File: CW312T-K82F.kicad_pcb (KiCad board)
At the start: 2 copper layers, 58.7 x 53.7 mm, 21 parts, among them J1 20_pin, P1 PCIEx4 EDGE CONNECTOR, U1 MK82FN256VLL15

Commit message: updated schematic and pcb - ready for review
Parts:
- moved R1 3.40 mm to (167.8, 86.7)
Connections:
- net /CW312T_Connector/nRST renamed nRST
- net /K82/JTAG_TCK renamed JTAG_TCK
- net /K82/JTAG_TDI renamed JTAG_TDI
- net /K82/JTAG_TDO renamed JTAG_TDO
- net /K82/JTAG_TMS renamed JTAG_TMS
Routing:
- net /CW312T_Connector/FILT_HP: track 35.0 -> 41.8 mm

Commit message: updated silkscreen and production files
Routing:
- net /CW312T_Connector/HDR1: track 22.1 -> 23.6 mm
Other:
- board text added: "K82F Target Board For ChipWhisperer CW312 Board"
- board text added: "RST"
- board text added: "VREF"
- board text removed: "K82F Target Board For ChipWhisperer CW312"
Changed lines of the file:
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@@
 		(tags "Surface mounted pin header SMD 2x10 1.00mm double row")
 		(property "Reference" "J1"
-			(at -2.85 -6.2 0)
+			(at -0.1 -6.25 0)
 			(layer "F.SilkS")
 			(effects
@@
 		)
 	)
+	(gr_line
+		(start 138.6 71)
+		(end 138.6 71.65)
+		(stroke
+			(width 0.15)
+			(type default)
+		)
+		(layer "B.SilkS")
+	)
+	(gr_line
+		(start 161.6 71.025)
+		(end 161.6 71.675)
+		(stroke
+			(width 0.15)
+			(type default)
+		)
+		(layer "F.SilkS")
+	)
 	(gr_text "NewAE Technology Inc. \nNAE-CW312T-K82F"
 		(at 154.8 92.25 0)
@@
 		)
 	)
-	(gr_text "K82F Target Board\nFor ChipWhisperer \nCW312"
-		(at 132.65 79.7 0)
+	(gr_text "RST"
+		(at 137.9 74.45 270)
+		(layer "B.SilkS")
+		(effects
+			(font
+				(size 1 1)
+				(thickness 0.15)
+			)
+			(justify left bottom mirror)
+		)
+	)
+	(gr_text "K82F Target Board\nFor ChipWhisperer \nCW312 Board"
+		(at 132.75 80.4 0)
 		(layer "F.SilkS")
 		(effects
@@
 		)
 	)
+	(gr_text "VREF"
+		(at 162.25 75.45 90)
+		(layer "F.SilkS")
+		(effects
+			(font
+				(size 1 1)
+				(thickness 0.15)
+			)
+			(justify left bottom)
+		)
+	)
 	(segment
 		(start 131.75 107.75)
@@
 		(start 167.024999 97.324999)
 		(end 167.6 97.9)
-		(width 0.3)
+		(width 0.2)
 		(layer "F.Cu")
 		(net 1)
@@
 		(start 165.575 97.324999)
 		(end 167.024999 97.324999)
-		(width 0.3)
+		(width 0.2)
 		(layer "F.Cu")
 		(net 1)
@@
 	)
 	(segment
-		(start 139.349997 74.449997)
-		(end 139.349997 92.302354)
+		(start 137.581545 73.644575)
+		(end 137.581545 73.681545)
 		(width 0.3)
 		(layer "F.Cu")
@@
 	)
 	(segment
-		(start 137.755 72.85)
-		(end 137.755 72.855)
+		(start 139.349997 75.449997)
+		(end 139.349997 92.302354)
 		(width 0.3)
 		(layer "F.Cu")
@@
 	)
 	(segment
-		(start 137.755 72.855)
-		(end 139.349997 74.449997)
+		(start 137.581545 73.681545)
+		(end 139.349997 75.449997)
 		(width 0.3)
 		(layer "F.Cu")
@@
 	)
 	(via
-		(at 137.755 72.85)
+		(at 137.581545 73.644575)
 		(size 0.6)
 		(drill 0.3)
@@
 	)
 	(segment
-		(start 137.755 72.85)
-		(end 137.605 72.7)
+		(start 137.605 73.62112)
+		(end 137.605 68.475)
 		(width 0.3)
 		(layer "B.Cu")
@@
 	)
 	(segment
-		(start 137.605 72.7)
-		(end 137.605 68.475)
+		(start 137.581545 73.644575)
+		(end 137.605 73.62112)
 		(width 0.3)
 		(layer "B.Cu")
@@
 	)
 	(segment
-		(start 156.9 86.75)
-		(end 156.9 88.149999)
+		(start 162.56788 76)
+		(end 162.56788 81.08212)
 		(width 0.3)
 		(layer "F.Cu")
@@
 	)
 	(segment
-		(start 162.56788 74.43712)
-		(end 162.56788 81.08212)
+		(start 156.9 86.75)
+		(end 156.9 88.149999)
 		(width 0.3)
 		(layer "F.Cu")
@@
 	)
 	(via
-		(at 162.56788 74.43712)
+		(at 162.56788 76)
 		(size 0.6)
 		(drill 0.3)
@@
 	)
 	(segment
-		(start 162.56788 74.43712)
-		(end 162.605 74.4)
+		(start 162.56788 76)
+		(end 162.605 75.96288)
 		(width 0.3)
 		(layer "B.Cu")
@@
 	)
 	(segment
-		(start 162.605 74.4)
-		(end 162.605 68.475)
+		(start 162.56788 74.51136)
+		(end 162.56788 76)
 		(width 0.3)
 		(layer "B.Cu")
@@
 	(segment
 		(start 162.605 74.47424)
-		(end 162.56788 74.43712)
+		(end 162.56788 74.51136)
+		(width 0.3)
+		(layer "B.Cu")
+		(net 22)
+	)
+	(segment
+		(start 162.605 75.96288)
+		(end 162.605 68.475)
 		(width 0.3)
 		(layer "B.Cu")
@@
 	)
 	(segment
-		(start 161.605 74.45)
-		(end 161.605 81.295)
+		(start 156.4 86.5)
+		(end 156.4 88.149999)
 		(width 0.3)
 		(layer "F.Cu")
@@
 	)
 	(segment
-		(start 156.4 86.5)
-		(end 156.4 88.149999)
+		(start 161.605 75.95)
+		(end 161.605 81.295)
 		(width 0.3)
 		(layer "F.Cu")
@@
 	)
 	(via
-		(at 161.605 74.45)
+		(at 161.605 75.95)
 		(size 0.6)
 		(drill 0.3)
@@
 	)
 	(segment
-		(start 161.605 74.45)
+		(start 161.605 75.95)
 		(end 161.605 68.475)
 		(width 0.3)
@@
 	)
 	(segment
-		(start 155.9 86.292894)
-		(end 155.9 88.149999)
+		(start 160.75 76)
+		(end 160.75 81.442894)
 		(width 0.3)
 		(layer "F.Cu")
@@
 	)
 	(segment
-		(start 160.75 74.45)
-		(end 160.75 81.442894)
+		(start 155.9 86.292894)
+		(end 155.9 88.149999)
 		(width 0.3)
 		(layer "F.Cu")
@@
 	)
 	(via
-		(at 160.75 74.45)
+		(at 160.75 76)
 		(size 0.6)
 		(drill 0.3)
@@
 	)
 	(segment
-		(start 160.75 74.45)
+		(start 160.75 76)
 		(end 160.75 68.57)
 		(width 0.3)
@@
 	)
 	(segment
-		(start 138.51788 74.53712)
-		(end 138.5 74.555)
-		(width 0.3)
-		(layer "F.Cu")
-		(net 83)
-	)
-	(segment
-		(start 138.5 74.555)
+		(start 138.5 75.51924)
 		(end 138.5 92.95)
 		(width 0.3)
@@
 	)
 	(segment
-		(start 140.6 95.05)
-		(end 140.6 95.1)
+		(start 138.5 92.95)
+		(end 140.6 95.05)
 		(width 0.3)
 		(layer "F.Cu")
@@
 	)
 	(segment
+		(start 138.44288 75.46212)
+		(end 138.5 75.51924)
+		(width 0.3)
+		(layer "F.Cu")
+		(net 83)
+	)
+	(segment
 		(start 163.824999 101.324999)
 		(end 165.575 101.324999)
@@
 	)
 	(segment
-		(start 138.5 92.95)
-		(end 140.6 95.05)
+		(start 155.65 78.3)
+		(end 155.6 78.25)
 		(width 0.3)
 		(layer "F.Cu")
@@
 	)
 	(segment
-		(start 155.65 78.3)
-		(end 155.6 78.25)
+		(start 140.6 95.05)
+		(end 140.6 95.1)
 		(width 0.3)
 		(layer "F.Cu")
@@
 	)
 	(via
-		(at 138.51788 74.53712)
+		(at 138.44288 75.46212)
 		(size 0.6)
 		(drill 0.3)
@@
 	)
 	(segment
-		(start 138.605 74.45)
-		(end 138.605 68.475)
+		(start 138.44288 75.46212)
+		(end 138.44288 75.05712)
+		(width 0.3)
+		(layer "B.Cu")
+		(net 83)
+	)
+	(segment
+		(start 138.44288 75.05712)
+		(end 138.605 74.895)
 		(width 0.3)
 		(layer "B.Cu")
@@
 	)
 	(segment
-		(start 138.51788 74.53712)
-		(end 138.605 74.45)
+		(start 149.95 103.45)
+		(end 152.15 101.25)
 		(width 0.3)
 		(layer "B.Cu")
@@
 	)
 	(segment
-		(start 149.95 103.45)
-		(end 152.15 101.25)
+		(start 138.605 74.895)
+		(end 138.605 68.475)
 		(width 0.3)
 		(layer "B.Cu")

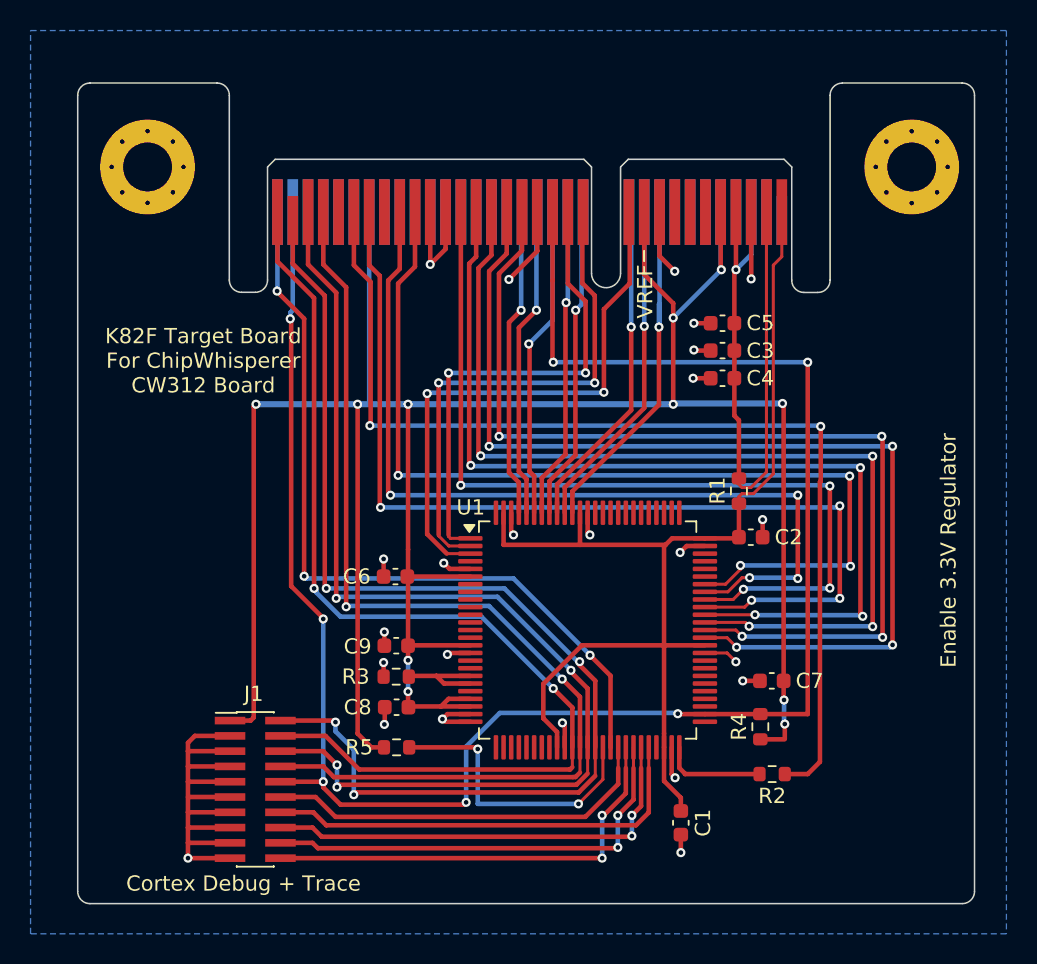
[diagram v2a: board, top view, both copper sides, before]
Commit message: updated schematic and pcb after library re-organization
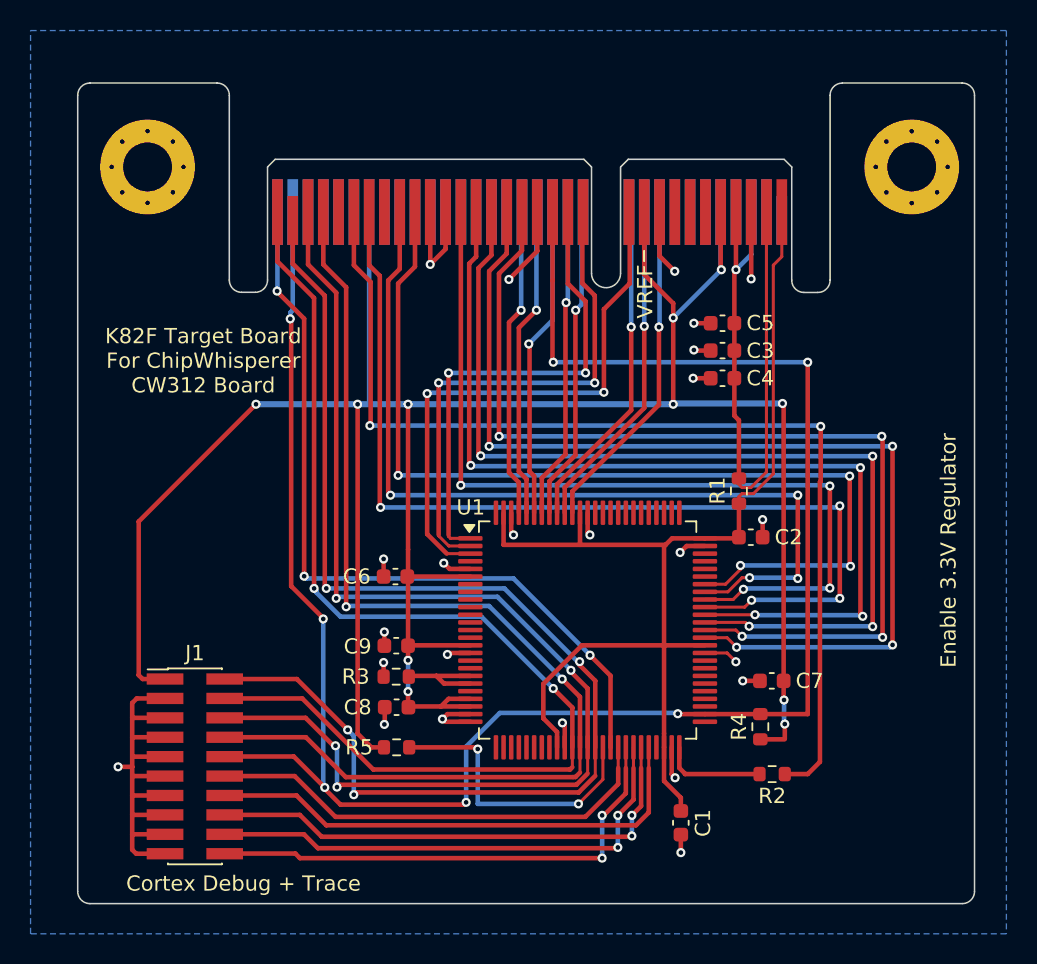
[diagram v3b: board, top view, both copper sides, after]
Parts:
- J1: footprint Connector_PinHeader_1.00mm:PinHeader_2x10_P1.00mm_Vertical_SMD -> Connector_PinHeader_1.27mm:PinHeader_2x10_P1.27mm_Vertical_SMD
- moved J1 4.23 mm to (132.2, 104.7)
- turned C1 to 90 degrees
- turned C2 to 180 degrees
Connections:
- C1 pad 1: /CW312T_Connector/SHUNTL -> GND
- C1 pad 2: GND -> /CW312T_Connector/SHUNTL
- C2 pad 1: /CW312T_Connector/SHUNTL -> GND
- C2 pad 2: GND -> /CW312T_Connector/SHUNTL
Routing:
- net JTAG_TDO: track 72.9 -> 78.2 mm
- net JTAG_TMS: track 76.8 -> 81.7 mm
- net JTAG_TCK: track 69.8 -> 74.5 mm
- net nRST: track 127.6 -> 132.2 mm
- net JTAG_TDI: track 69.3 -> 73.6 mm
- net /K82/TRACECLK: track 25.9 -> 30.1 mm
- net /K82/TRACED0: track 29.1 -> 33.2 mm
- net /K82/TRACED2: track 29.3 -> 33.1 mm
- net /K82/TRACED1: track 29.5 -> 33.3 mm
- net /K82/TRACED3: track 29.0 -> 32.8 mm
- net GND: track 82.4 -> 80.1 mm
- net /CW312T_Connector/HDR1: track 23.6 -> 22.0 mm
- net VCC: track 176.8 -> 177.3 mm
